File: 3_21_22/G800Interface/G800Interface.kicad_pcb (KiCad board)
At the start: 2 copper layers, 34 parts, among them J1 11pin G800 Conn., J2 USB_C_Receptacle_USB2.0, U1 FT232RL

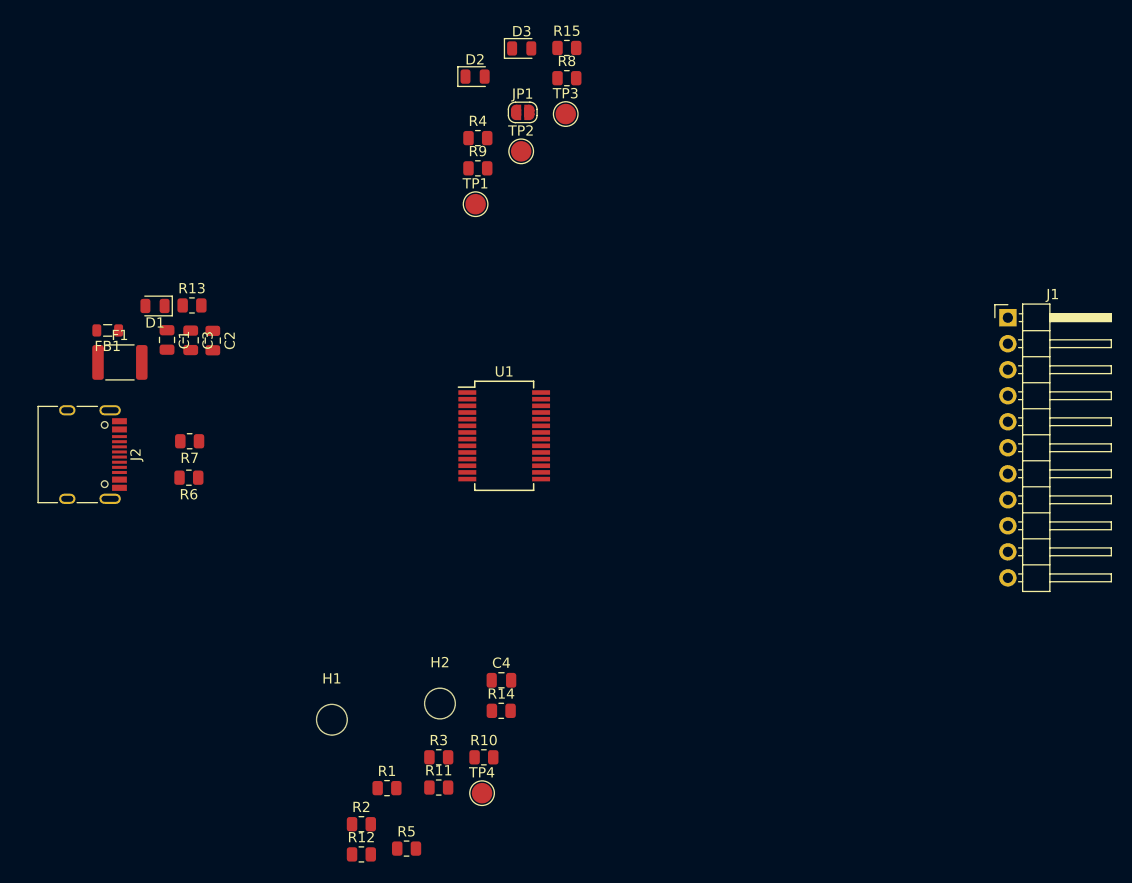
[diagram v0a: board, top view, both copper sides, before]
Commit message: diff pair + decoupling C
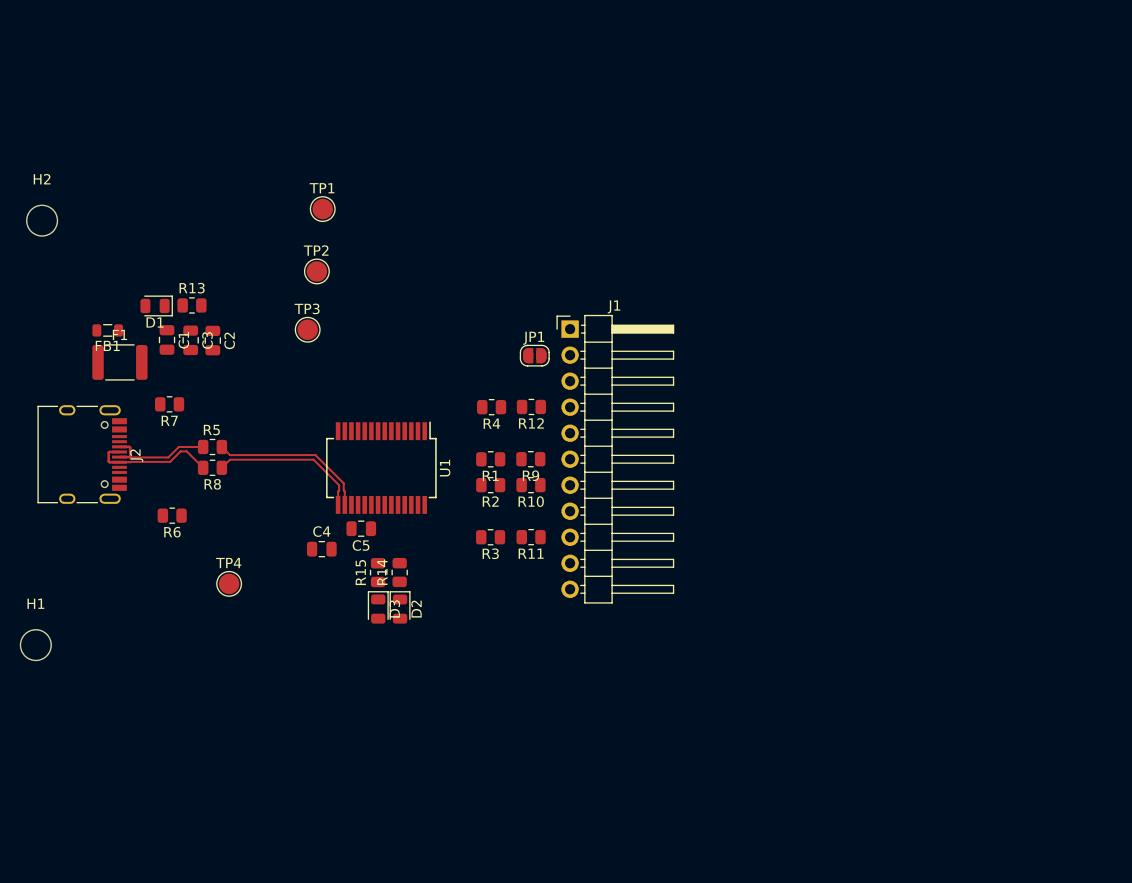
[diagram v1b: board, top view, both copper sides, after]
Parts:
- added C5: 0.1uF, Capacitor_SMD:C_0805_2012Metric, F.Cu at (111.4, 94.1)
- moved H2 61.1 mm to (80.3, 64.1)
- moved D3 56.5 mm to (113.1, 102.0), turned to 270 degrees
- moved R15 54.4 mm to (113.1, 98.4), turned to 90 degrees
- moved D2 52.5 mm to (115.2, 102.0), turned to 270 degrees
- moved R8 51.4 mm to (96.9, 88.2), turned to 180 degrees
- moved R12 46.7 mm to (128.0, 82.2), turned to 180 degrees
- moved R5 43.5 mm to (96.9, 86.2), turned to 180 degrees
- moved J1 42.8 mm to (131.8, 74.7)
- moved R2 35.4 mm to (124.1, 89.9), turned to 180 degrees
- moved R1 33.7 mm to (124.1, 87.4), turned to 180 degrees
- moved TP3 32.8 mm to (106.2, 74.7)
- moved TP4 32.1 mm to (98.5, 99.5)
- moved H1 29.8 mm to (79.7, 105.5)
- moved R9 28.9 mm to (128.0, 87.3), turned to 180 degrees
- moved R10 27.0 mm to (128.0, 89.9), turned to 180 degrees
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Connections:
- net Net-(J2-PadA6) renamed /D+
- net Net-(J2-PadA7) renamed /D-
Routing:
- net USBD-: track 0.00 -> 15.5 mm
- net USBD+: track 0.00 -> 14.8 mm
- net /D+: track 0.00 -> 12.3 mm
- net /D-: track 0.00 -> 11.6 mm

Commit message: finished G800
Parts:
- TP1, TP2, TP3, TP4: moved to B.Cu
- moved TP3 24.1 mm to (99.0, 97.7)
- moved TP1 21.2 mm to (97.2, 81.4)
- moved TP2 20.6 mm to (88.8, 78.5)
- moved H2 7.60 mm to (85.0, 70.0)
- moved TP4 7.27 mm to (95.7, 92.8)
- moved JP1 7.12 mm to (121.5, 75.3)
- moved H1 6.99 mm to (85.0, 101.0)
- moved R1 6.94 mm to (117.4, 85.4)
- moved R2 6.94 mm to (117.4, 87.9)
- moved D2 6.94 mm to (108.5, 100.0)
- moved D3 6.94 mm to (106.4, 100.0)
- moved J1 6.94 mm to (125.1, 72.7)
- moved U1 6.94 mm to (106.7, 86.3)
- moved R10 6.94 mm to (121.3, 87.9)
- moved R11 6.94 mm to (121.3, 93.0)
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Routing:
- net VCCIO: track 0.00 -> 76.8 mm, vias 0 -> 1
- net GND: track 0.00 -> 32.3 mm, vias 0 -> 40
- net VBUS: track 0.00 -> 19.6 mm, vias 0 -> 1
- net Net-(R4-Pad2): track 0.00 -> 13.9 mm
- net Net-(R3-Pad2): track 0.00 -> 13.6 mm
- net Net-(R2-Pad2): track 0.00 -> 12.8 mm, vias 0 -> 2
- net +3V3: track 0.00 -> 11.2 mm, vias 0 -> 1
- net CTSCalc: track 0.00 -> 7.98 mm
- net USBD-: track 15.5 -> 7.80 mm
- net TXDCalc: track 0.00 -> 7.69 mm
- net RXDCalc: track 0.00 -> 7.69 mm
- net USBD+: track 14.8 -> 7.09 mm
- net RTSCalc: track 0.00 -> 7.62 mm
- net Net-(R1-Pad2): track 0.00 -> 6.67 mm
- net TXLED: track 0.00 -> 6.02 mm
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- added copper zone on B.Cu, net GND
- added copper zone on F.Cu, net GND
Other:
- board outline added: 46 x 39 mm
- net class Default: via_dia 0.8 -> 0.6; via_drill 0.4 -> 0.3
- net class PWR added: clearance 0.2, trace_width 0.4, via_dia 0.6, via_drill 0.3
- board text added: "+3.3V"
- board text added: "+5V"
- board text added: "GND"
- board text added: "USBC to G800 Interface"
- board text added: "VBUS"
- board text added: "VCC Connect"
- board text added: "ИУ10"
